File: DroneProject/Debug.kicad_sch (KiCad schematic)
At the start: 18 parts

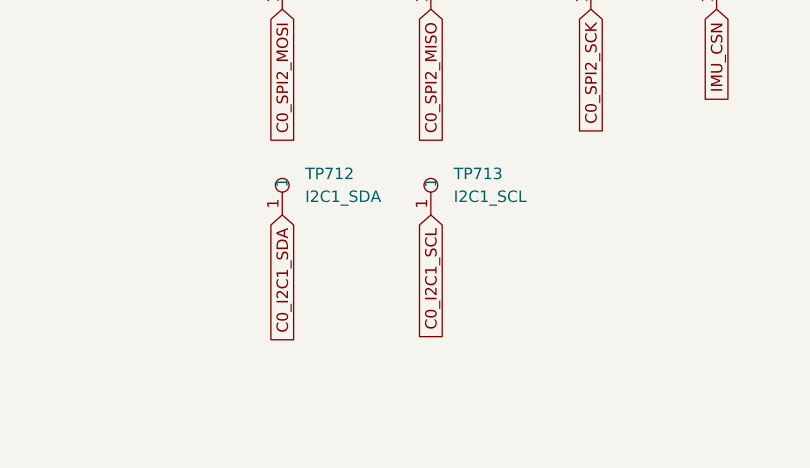
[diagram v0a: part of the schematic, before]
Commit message: Finished layout for controller board
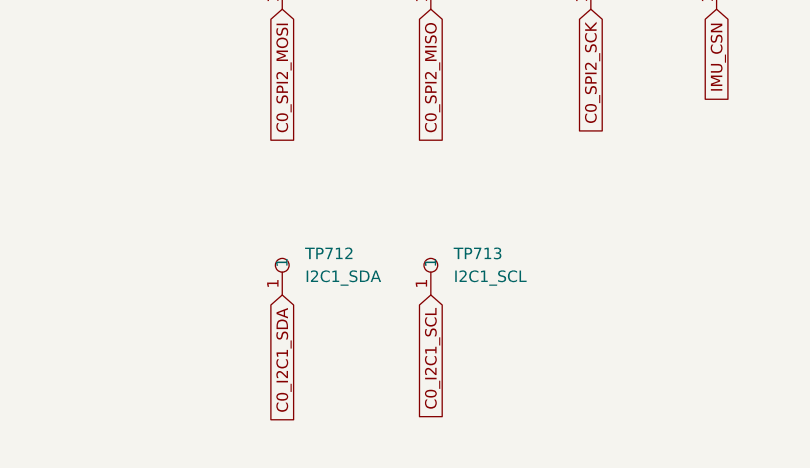
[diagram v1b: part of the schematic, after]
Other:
- moved on the sheet: TP712, TP713
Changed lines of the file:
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@@
 	(global_label "C0_I2C1_SCL"
 		(shape input)
-		(at 147.32 106.68 270)
-		(fields_autoplaced yes)
-		(effects
-			(font
-				(size 1.27 1.27)
-			)
-			(justify right)
-		)
-		(property "Intersheetrefs" "${INTERSHEET_REFS}"
-			(at 147.32 121.8813 90)
+		(at 147.32 115.57 270)
+		(fields_autoplaced yes)
+		(effects
+			(font
+				(size 1.27 1.27)
+			)
+			(justify right)
+		)
+		(property "Intersheetrefs" "${INTERSHEET_REFS}"
+			(at 147.32 130.7713 90)
 			(effects
 				(font
@@
 	(global_label "C0_I2C1_SDA"
 		(shape input)
-		(at 130.81 106.68 270)
-		(fields_autoplaced yes)
-		(effects
-			(font
-				(size 1.27 1.27)
-			)
-			(justify right)
-		)
-		(property "Intersheetrefs" "${INTERSHEET_REFS}"
-			(at 130.81 121.9418 90)
+		(at 130.81 115.57 270)
+		(fields_autoplaced yes)
+		(effects
+			(font
+				(size 1.27 1.27)
+			)
+			(justify right)
+		)
+		(property "Intersheetrefs" "${INTERSHEET_REFS}"
+			(at 130.81 130.8318 90)
 			(effects
 				(font
@@
 	(symbol
 		(lib_id "Global:Testpoint")
-		(at 130.81 106.68 0)
+		(at 130.81 115.57 0)
 		(unit 1)
 		(exclude_from_sim no)
@@
 		(fields_autoplaced yes)
 		(property "Reference" "TP712"
-			(at 133.35 102.1079 0)
+			(at 133.35 110.9979 0)
 			(effects
 				(font
@@
 		)
 		(property "Value" "I2C1_SDA"
-			(at 133.35 104.6479 0)
+			(at 133.35 113.5379 0)
 			(effects
 				(font
@@
 		)
 		(property "Footprint" "Library:Testpoint 1.6mm x 0.8mm"
-			(at 130.81 106.68 0)
+			(at 130.81 115.57 0)
 			(effects
 				(font
@@
 		)
 		(property "Datasheet" ""
-			(at 130.81 106.68 0)
+			(at 130.81 115.57 0)
 			(effects
 				(font
@@
 		)
 		(property "Description" ""
-			(at 130.81 106.68 0)
+			(at 130.81 115.57 0)
 			(effects
 				(font
@@
 	(symbol
 		(lib_id "Global:Testpoint")
-		(at 147.32 106.68 0)
+		(at 147.32 115.57 0)
 		(unit 1)
 		(exclude_from_sim no)
@@
 		(fields_autoplaced yes)
 		(property "Reference" "TP713"
-			(at 149.86 102.1079 0)
+			(at 149.86 110.9979 0)
 			(effects
 				(font
@@
 		)
 		(property "Value" "I2C1_SCL"
-			(at 149.86 104.6479 0)
+			(at 149.86 113.5379 0)
 			(effects
 				(font
@@
 		)
 		(property "Footprint" "Library:Testpoint 1.6mm x 0.8mm"
-			(at 147.32 106.68 0)
+			(at 147.32 115.57 0)
 			(effects
 				(font
@@
 		)
 		(property "Datasheet" ""
-			(at 147.32 106.68 0)
+			(at 147.32 115.57 0)
 			(effects
 				(font
@@
 		)
 		(property "Description" ""
-			(at 147.32 106.68 0)
-			(effects
-				(font
+			(at 147.32 115.57 0)
+			(effects
+				(font
